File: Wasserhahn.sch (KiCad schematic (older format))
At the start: 18 parts, among them J1 Mains, J2 Ball_Valve_Contacts, J3 ToRelais, J4 PRGM_ADAPTER, J5 Boot/PRGM, U1 ESP-WROOM-02

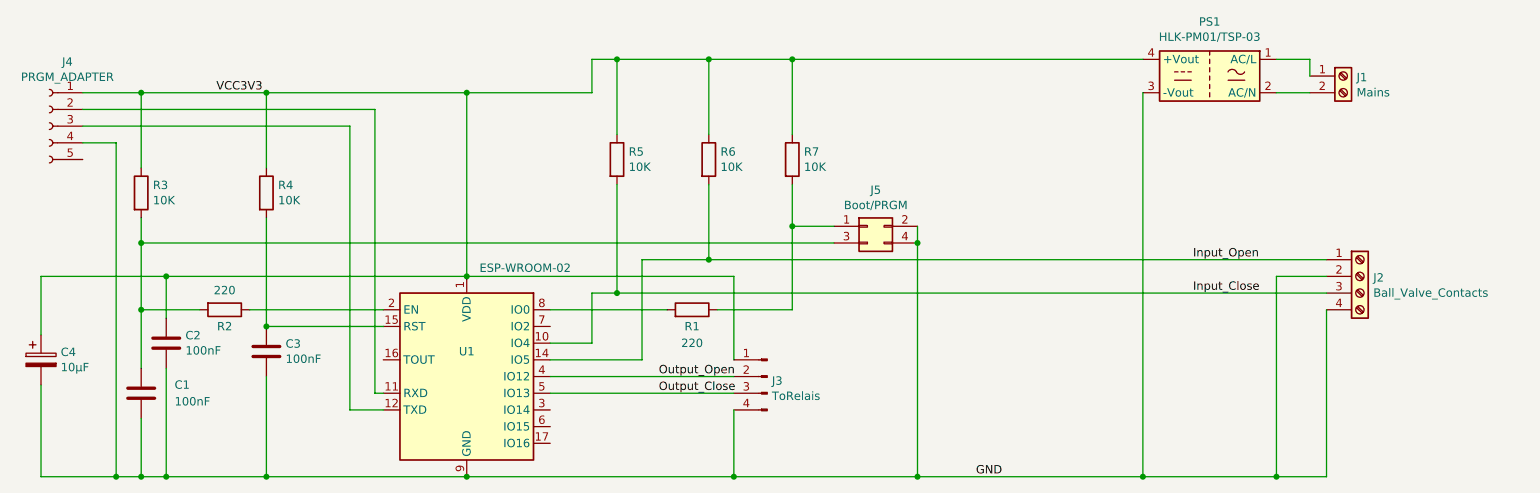
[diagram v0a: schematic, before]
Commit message: added connections for IO2, removed short circuit, swaped EN and RST on Jumper
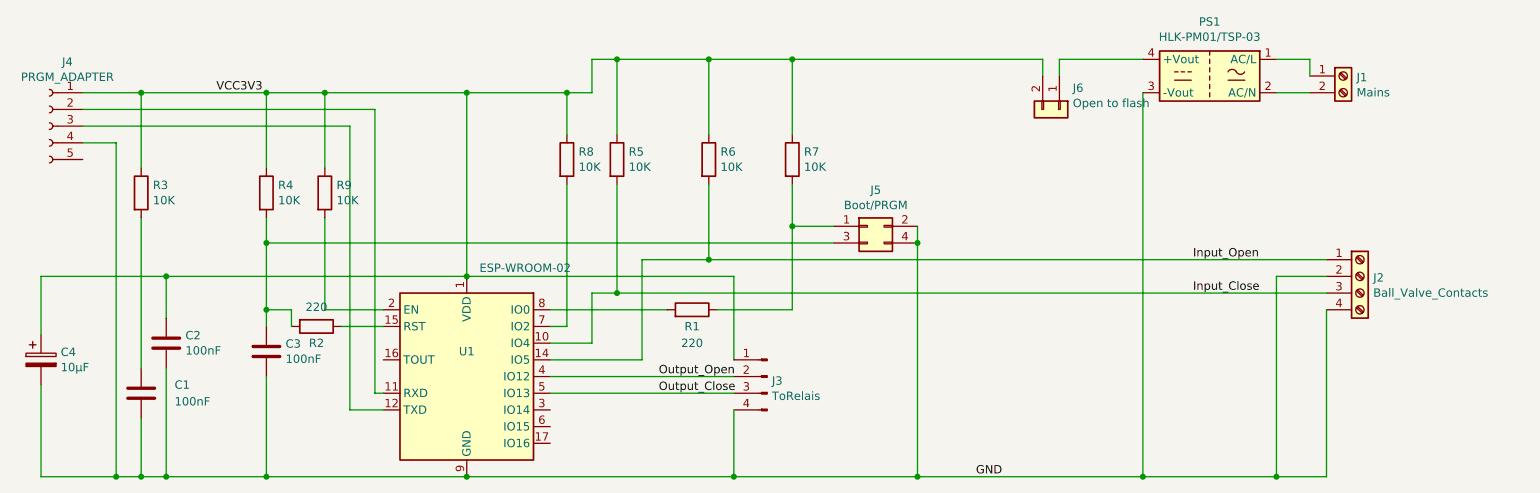
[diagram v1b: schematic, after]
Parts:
- added J6: Open to flash, Connector_PinHeader_2.54mm:PinHeader_1x02_P2.54mm_Horizontal, symbol Connector_Generic:Conn_01x02
- added R8, R9: 10K, Resistor_THT:R_Axial_DIN0207_L6.3mm_D2.5mm_P10.16mm_Horizontal, symbol Device:R
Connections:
- net VCC3V3: now also J6.2 (Pin_2), R8.1, R9.1; no longer PS1.4 (+Vout)
- net at C3.1, R4.2: now also J5.3 (Pin_3), R2.2; no longer U1.15 (RST)
- net at R2.1: now also U1.15 (RST); no longer U1.2 (EN)
- net at U1.7 (IO2): now also R8.2
- net at C1.1, R3.2: no longer J5.3 (Pin_3), R2.2
- new net: R9.2, U1.2 (EN)
- new net: J6.1 (Pin_1), PS1.4 (+Vout)
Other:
- moved on the sheet: R2
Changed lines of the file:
@@
 Connection ~ 2750 3500
-Wire Wire Line
-	2750 2600 3450 2600
 Wire Wire Line
 	2150 2550 2150 2300
@@
 	5550 2300 3950 2300
 Wire Wire Line
-	3950 1200 4700 1200
+	3950 1200 4550 1200
 Connection ~ 3950 1200
 Wire Wire Line
@@
 	5000 2800 4450 2800
 Wire Wire Line
-	2750 1950 2750 2600
-Connection ~ 2750 2600
+	2750 1950 2750 2100
 Wire Wire Line
 	2750 1650 2750 1200
@@
 	8000 3500 8800 3500
 Wire Wire Line
-	8000 1000 5900 1000
-Wire Wire Line
 	4700 1000 4700 1200
 Wire Wire Line
@@
 L Device:R R2
 U 1 1 5EAA2734
-P 2500 2500
-F 0 "R2" V 2600 2500 50  0000 C CNN
-F 1 "220" V 2384 2500 50  0000 C CNN
-F 2 "Resistor_THT:R_Axial_DIN0207_L6.3mm_D2.5mm_P10.16mm_Horizontal" V 2430 2500 50  0001 C CNN
-F 3 "~" H 2500 2500 50  0001 C CNN
-	1    2500 2500
+P 3050 2600
+F 0 "R2" V 3150 2600 50  0000 C CNN
+F 1 "220" V 2934 2600 50  0000 C CNN
+F 2 "Resistor_THT:R_Axial_DIN0207_L6.3mm_D2.5mm_P10.16mm_Horizontal" V 2980 2600 50  0001 C CNN
+F 3 "~" H 3050 2600 50  0001 C CNN
+	1    3050 2600
 	0    1    1    0
 $EndComp
@@
 Wire Wire Line
 	1850 1500 1850 3500
-Connection ~ 5900 1000
 Wire Wire Line
 	5900 1000 5400 1000
@@
 	2000 1200 2750 1200
 Wire Wire Line
-	2750 1200 3950 1200
+	2750 1200 3100 1200
 Connection ~ 2000 3500
 Wire Wire Line
@@
 Wire Wire Line
 	2750 3500 3950 3500
-Wire Wire Line
-	2650 2500 3450 2500
-Wire Wire Line
-	2350 2500 2000 2500
-Connection ~ 2000 2500
-Wire Wire Line
-	2000 2500 2000 2850
 Wire Wire Line
 	6650 2000 6650 2100
@@
 	5400 2200 5000 2200
 Wire Wire Line
-	2000 1950 2000 2100
-Wire Wire Line
-	6150 2100 2000 2100
-Connection ~ 2000 2100
-Wire Wire Line
-	2000 2100 2000 2500
+	6150 2100 2750 2100
+Connection ~ 2750 2100
+Wire Wire Line
+	2750 2100 2750 2500
+Wire Wire Line
+	2000 1950 2000 2850
+Wire Wire Line
+	3450 2600 3200 2600
+Wire Wire Line
+	2900 2600 2900 2500
+Wire Wire Line
+	2900 2500 2750 2500
+Connection ~ 2750 2500
+Wire Wire Line
+	2750 2500 2750 2600
+$Comp
+L Device:R R9
+U 1 1 5EC1253C
+P 3100 1800
+F 0 "R9" H 3170 1846 50  0000 L CNN
+F 1 "10K" H 3170 1755 50  0000 L CNN
+F 2 "Resistor_THT:R_Axial_DIN0207_L6.3mm_D2.5mm_P10.16mm_Horizontal" V 3030 1800 50  0001 C CNN
+F 3 "~" H 3100 1800 50  0001 C CNN
+	1    3100 1800
+	1    0    0    -1
+$EndComp
+Wire Wire Line
+	3450 2500 3100 2500
+Wire Wire Line
+	3100 2500 3100 1950
+Wire Wire Line
+	3100 1650 3100 1200
+Connection ~ 3100 1200
+Wire Wire Line
+	3100 1200 3950 1200
+$Comp
+L Device:R R8
+U 1 1 5EC16764
+P 4550 1600
+F 0 "R8" H 4620 1646 50  0000 L CNN
+F 1 "10K" H 4620 1555 50  0000 L CNN
+F 2 "Resistor_THT:R_Axial_DIN0207_L6.3mm_D2.5mm_P10.16mm_Horizontal" V 4480 1600 50  0001 C CNN
+F 3 "~" H 4550 1600 50  0001 C CNN
+	1    4550 1600
+	1    0    0    -1
+$EndComp
+Wire Wire Line
+	4450 2600 4550 2600
+Wire Wire Line
+	4550 2600 4550 1750
+Wire Wire Line
+	4550 1450 4550 1200
+Connection ~ 4550 1200
+Wire Wire Line
+	4550 1200 4700 1200
+$Comp
+L Connector_Generic:Conn_01x02 J6
+U 1 1 5EC1D020
+P 7500 1300
+F 0 "J6" V 7372 1380 50  0000 L CNN
+F 1 "Open to flash" V 7463 1380 50  0000 L CNN
+F 2 "Connector_PinHeader_2.54mm:PinHeader_1x02_P2.54mm_Horizontal" H 7500 1300 50  0001 C CNN
+F 3 "~" H 7500 1300 50  0001 C CNN
+	1    7500 1300
+	0    1    1    0
+$EndComp
+Wire Wire Line
+	8000 1000 7500 1000
+Wire Wire Line
+	7500 1000 7500 1100
+Wire Wire Line
+	7400 1100 7400 1000
+Wire Wire Line
+	7400 1000 5900 1000
+Connection ~ 5900 1000
 $EndSCHEMATC

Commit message: GPIO15 pulled low, jumper to disconnect Power for flashing
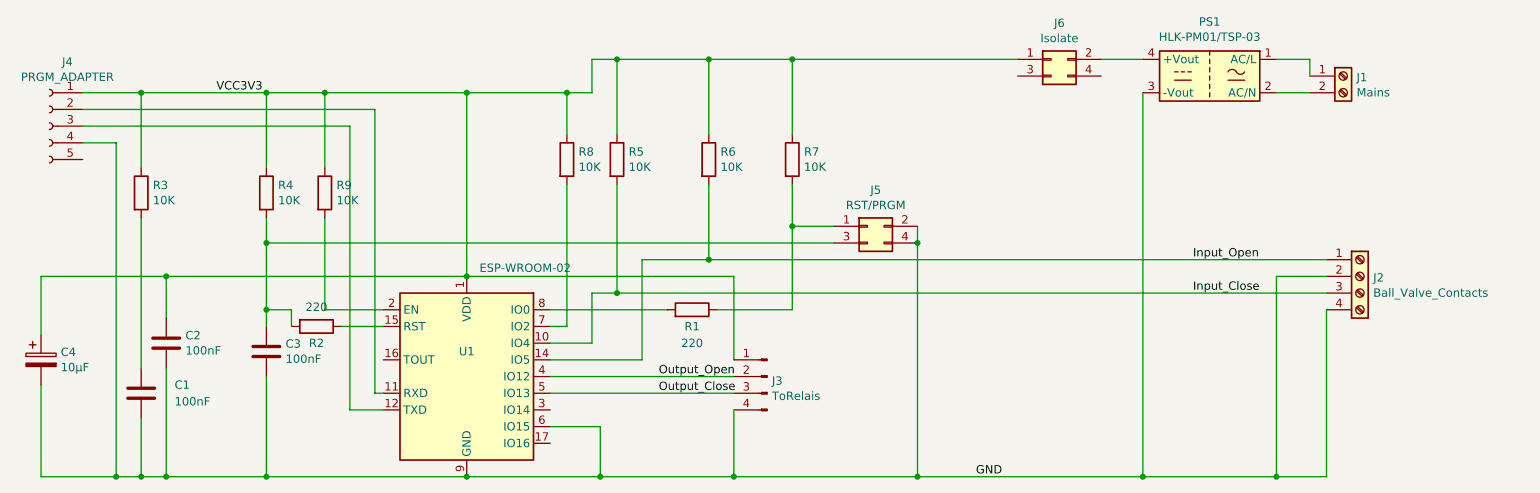
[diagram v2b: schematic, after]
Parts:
- removed J6: Open to flash, Connector_PinHeader_2.54mm:PinHeader_1x02_P2.54mm_Horizontal, symbol Connector_Generic:Conn_01x02
- added J6: Isolate, Connector_PinHeader_2.54mm:PinHeader_2x02_P2.54mm_Vertical, symbol Connector_Generic:Conn_02x02_Odd_Even
- J5: value Boot/PRGM -> RST/PRGM
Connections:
- net GND: now also U1.6 (IO15)
- net VCC3V3: now also J6.1 (Pin_1)
- net at PS1.4 (+Vout): now also J6.2 (Pin_2)
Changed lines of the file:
@@
 P 6350 2000
 F 0 "J5" H 6400 2217 50  0000 C CNN
-F 1 "Boot/PRGM" H 6400 2126 50  0000 C CNN
+F 1 "RST/PRGM" H 6400 2126 50  0000 C CNN
 F 2 "Connector_PinHeader_2.54mm:PinHeader_2x02_P2.54mm_Vertical" H 6350 2000 50  0001 C CNN
 F 3 "~" H 6350 2000 50  0001 C CNN
@@
 	5550 3100 5550 3500
 Wire Wire Line
-	5550 3500 3950 3500
+	5550 3500 4750 3500
 Connection ~ 3950 3500
 Wire Wire Line
@@
 Wire Wire Line
 	4550 1200 4700 1200
-$Comp
-L Connector_Generic:Conn_01x02 J6
-U 1 1 5EC1D020
-P 7500 1300
-F 0 "J6" V 7372 1380 50  0000 L CNN
-F 1 "Open to flash" V 7463 1380 50  0000 L CNN
-F 2 "Connector_PinHeader_2.54mm:PinHeader_1x02_P2.54mm_Horizontal" H 7500 1300 50  0001 C CNN
-F 3 "~" H 7500 1300 50  0001 C CNN
-	1    7500 1300
-	0    1    1    0
-$EndComp
-Wire Wire Line
-	8000 1000 7500 1000
-Wire Wire Line
-	7500 1000 7500 1100
-Wire Wire Line
-	7400 1100 7400 1000
-Wire Wire Line
-	7400 1000 5900 1000
 Connection ~ 5900 1000
+Wire Wire Line
+	4450 3200 4750 3200
+Wire Wire Line
+	4750 3200 4750 3500
+Connection ~ 4750 3500
+Wire Wire Line
+	4750 3500 3950 3500
+$Comp
+L Connector_Generic:Conn_02x02_Odd_Even J6
+U 1 1 5EC5C94F
+P 7450 1000
+F 0 "J6" H 7500 1217 50  0000 C CNN
+F 1 "Isolate" H 7500 1126 50  0000 C CNN
+F 2 "Connector_PinHeader_2.54mm:PinHeader_2x02_P2.54mm_Vertical" H 7450 1000 50  0001 C CNN
+F 3 "~" H 7450 1000 50  0001 C CNN
+	1    7450 1000
+	1    0    0    -1
+$EndComp
+Wire Wire Line
+	7750 1000 8000 1000
+Wire Wire Line
+	5900 1000 7250 1000
 $EndSCHEMATC
